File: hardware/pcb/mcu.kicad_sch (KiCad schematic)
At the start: 15 parts, among them J3 FSR pads, U1 ESP32-WROOM-32E-N8R2, U18 W25Q512JVEIQ, U19 TCA6408ARSVR

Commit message: Improve hw_v2 PCB: HV tail chains, decoupling re-park, power islands, U22 escape
Schematic fixes:
- Fix SWEAT_RE silently shorted to GND (D27 pin-endpoint collision)
- Fix L2/TX_5V boost miswire (VBAT_SYS->TX_SW, rail was dead)
- Add J11/J13 HV-boundary chains: R118-R122 2512 cut-points + D26-D30 DNP TPD clamps
- Correct J12 to FH12-14S-0.5SH land; R114 LED_AN fed from TX_5V
- Move U24 VBACKUP to dedicated RTC_VBK net; ADS1292 CLK grounded
- Add CS pull-ups (R115-R117), TP28, C84 (U4 +3V3 input decoupling)
- New hw_v2 parts: U22 MAX86178, U23 SHT45, U24 RTC (DNP), U25 IM69D130 (DNP),
  D12 SFH4735 NIR + Q4 gate, J9-J13 tails

Layout:
- Grow board 32->40 mm east; five 2512 HV parts could not fit at 32 mm
- Re-park ~30 decoupling passives adjacent to their ICs
- Replace phantom moat wall slots with a real >=1.0 mm channel
- Own-layer pour keepouts under HV pads; wider stitch-via HV margin
- U22 WLP: drop 28 NC lands (rows B-E) to open B.Cu escape for F-row
- Retarget dead power islands (TX_5V over its 9 loads, +1V8 under LDO, +3V3 at U7)

BOM/CPL: footprint-aware 0R mapping (0402->C17168, 2512->C2908946),
DNP parts excluded, J11/J13 pads DNP'd, U1 MPN corrected.

Gates: placement zero (291 parts), ERC 0, DRC non-unrouted 0
(9 inherent Q1/Q2/Q4 intra-package clearances waived-by-name).
Board remains unrouted by design - research prototype, not fab-ready.

Generated with [Devin](https://devin.ai)

Co-Authored-By: Devin <158243242+devin-ai-integration[bot]@users.noreply.github.com>
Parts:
- removed U1: ESP32-WROOM-32E-N8R2, RF_Module:ESP32-WROOM-32E, symbol vitalq:ESP32-WROOM-32E-R2
- added C78: 100n, Capacitor_SMD:C_0402_1005Metric, symbol vitalq:C
- added R107, R108: 100k, Resistor_SMD:R_0402_1005Metric, symbol vitalq:R
- added U1: ESP32-S3-MINI-1U-N4R2, vitalq:ESP32_S3_MINI_1U, symbol vitalq:ESP32-S3-MINI-1U-N4R2
- added U25: IM69D130, vitalq:IM69D130, symbol vitalq:IM69D130
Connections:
- net +3V3: now also C78.1, U25.2 (VDD)
- net +3V3_ESP: now also U1.3 (3V3)
- net AD5940_GPIO0: now also U1.18 (IO14)
- net ADS1292_DRDY: now also U1.6 (IO2)
- net AFE4900_ADC_RDY: now also U1.25 (IO21)
- net CHG_PG: now also U1.11 (IO7)
- net CS_AD5940: now also U1.19 (IO15)
- net CS_ADS1292: now also U1.14 (IO10)
- net CS_AFE4900: now also U1.22 (IO18)
- net CS_FLASH: now also U1.20 (IO16)
- net ESP_EN: now also U1.45 (EN)
- net ESP_IO0: now also U1.4 (IO0)
- net ESP_RX: now also U1.40 (RXD0)
- net ESP_TX: now also U1.39 (TXD0)
- net EXP_INT: now also U1.7 (IO3)
- net FSR_ADC: now also U1.5 (IO1)
- net GAUGE_ALRT: now also U1.10 (IO6)
- net GND: now also C78.2, R108.2, U1.1 (GND), U1.2 (GND), U1.42 (GND), U1.43 (GND), U1.46 (GND), U1.47 (GND), U1.48 (GND), U1.49 (GND), U1.50 (GND), U1.51 (GND), U1.52 (GND), U1.53 (GND), U1.54 (GND), U1.55 (GND), U1.56 (GND), U1.57 (GND), U1.58 (GND), U1.59 (GND), U1.60 (GND), U1.61 (GND), U1.62 (GND), U1.63 (GND), U1.64 (GND), U1.65 (GND), U25.4 (SELECT), U25.5 (GND)
- net I2C_SCL: now also U1.13 (IO9)
- net I2C_SDA: now also U1.12 (IO8)
- net LSM6_INT1: now also U1.8 (IO4)
- net SPI_MISO: now also U1.17 (IO13)
- net SPI_MOSI: now also U1.15 (IO11)
- net SPI_SCK: now also U1.16 (IO12)
- net STATUS_LED: now also U1.21 (IO17)
- net TMP117_ALERT: now also U1.9 (IO5)
- new net CS_MAX86178: U1.34 (IO38)
- new net MAX86178_INT: U1.35 (IO39)
- new net MIC_CLK: U1.36 (IO40), U25.3 (CLOCK)
- new net MIC_DAT: U1.37 (IO41), U25.1 (DATA)
- new net SPARE_IN: R107.2, R108.1, U1.38 (IO42)
- new net USB_DM_S3: U1.23 (IO19)
- new net USB_DP_S3: U1.24 (IO20)
- new net VBAT: R107.1
- no-connect marks 3 -> 10
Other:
- note added: "ESP32-S3-MINI-1U-N4R2. U.FL antenna: the x<6.5 mm keep-out is gone. 4 MB flash + 2 MB PSRAM inside."
- note added: "IO0 is the boot strap (SW2, R6). IO3 is JTAG-sel; R53 holds EXP_INT high. IO45/IO46 left unstrapped."
- note added: "IO26 is the in-module PSRAM select on N4R2. IO33-37, IO47, IO48 are spare GPIO, left open."
- note added: "R7 keeps CS_AD5940 high at reset. CS pull-ups R52/R98 unchanged; IO15 is not an S3 strap."
- note added: "SPARE_IN: IO42 digital-only; DNP divider = logic VBAT detect only."
- note added: "U25 IM69D130, DNP. PDM on IO40/IO41. 100 nF on VDD (datasheet)."
- note removed: "ESP32-WROOM-32E-N8R2. GPIO16 is PSRAM and stays inside the module."
- note removed: "GPIO2 and GPIO12 are open so the straps stay low. GPIO15 (CS_AD5940) is pulled up."
- note removed: "GPIO6-11 are the module flash bus and have no symbol pins. ADC1 is GPIO36 and GPIO39."
- note removed: "R7 is the only chip-select pull-up. It is required because GPIO15 must be high at reset."

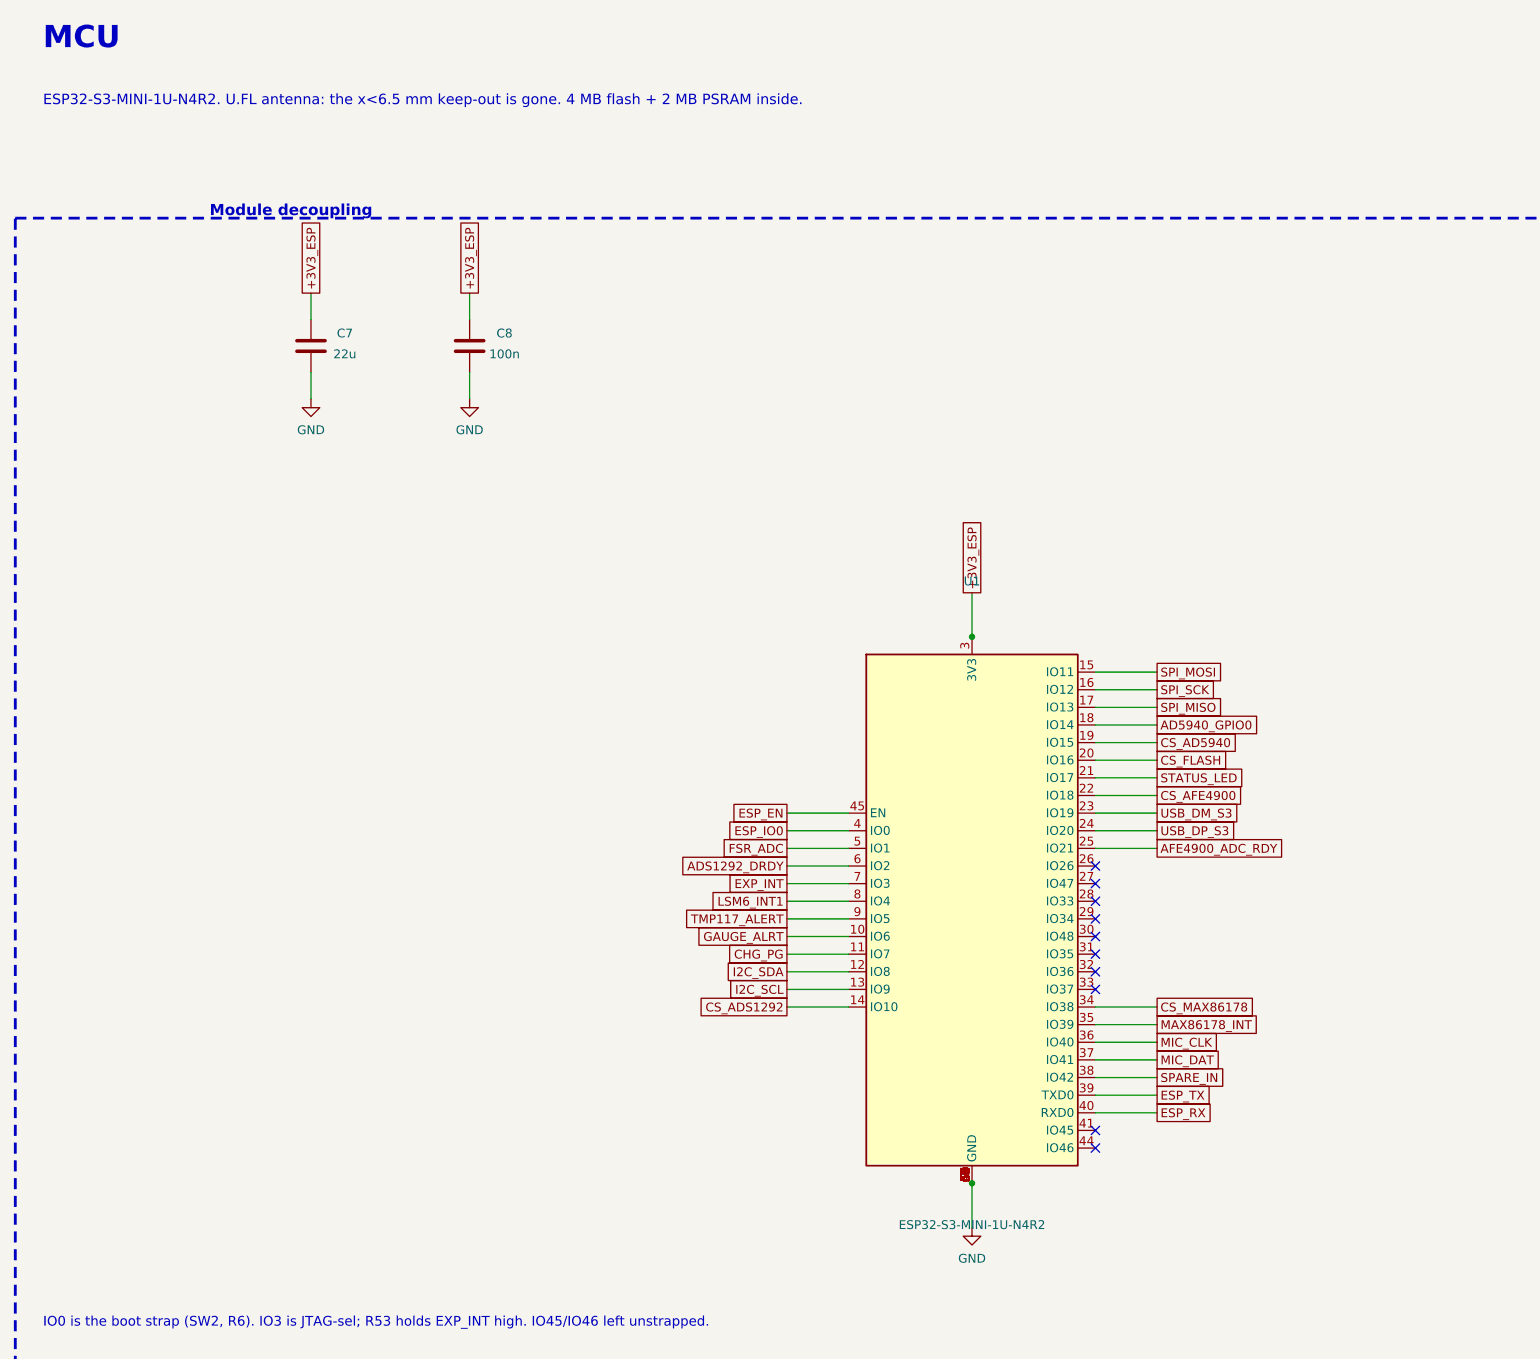
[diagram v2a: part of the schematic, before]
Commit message: Switch U1 to ESP32-S3-MINI-1-N4R2 (integrated PCB antenna)
- design.py: FP_S3 -> vitalq:ESP32_S3_MINI_1; MINI-1 shares the MINI-1U
  65-pad map and N4R2 memory, adds a 5.1 mm pad-free antenna tab
- footprint renamed/extended: outline 15.4x20.5 mm, antenna at local -Y;
  tab overhangs board top edge ~2.8 mm at U1 (12.4, 10.0) rot 0
- build_pcb.py: ufl_dress zone -> antenna_keepout rule area
  (x4.55-20.25, y0-2.45, all copper; no tracks/vias/pads/pours)
- board_finish.py: stitch-via blocklist covers antenna region
- relocations: J9 -> east edge (38.8,15.0,rot90); R7/R70/R71/R72 moved
  out of the keepout band
- BOM/JLC: U1 -> ESP32-S3-MINI-1-N4R2, LCSC C3013941

check.sh: PASS — ERC 0; clashes/edge/pth/pad-miss 0; DRC = 499 unrouted
items only (no keepout violations); 0 vias in antenna zone.

Generated with [Devin](https://devin.ai)

Co-Authored-By: Devin <158243242+devin-ai-integration[bot]@users.noreply.github.com>
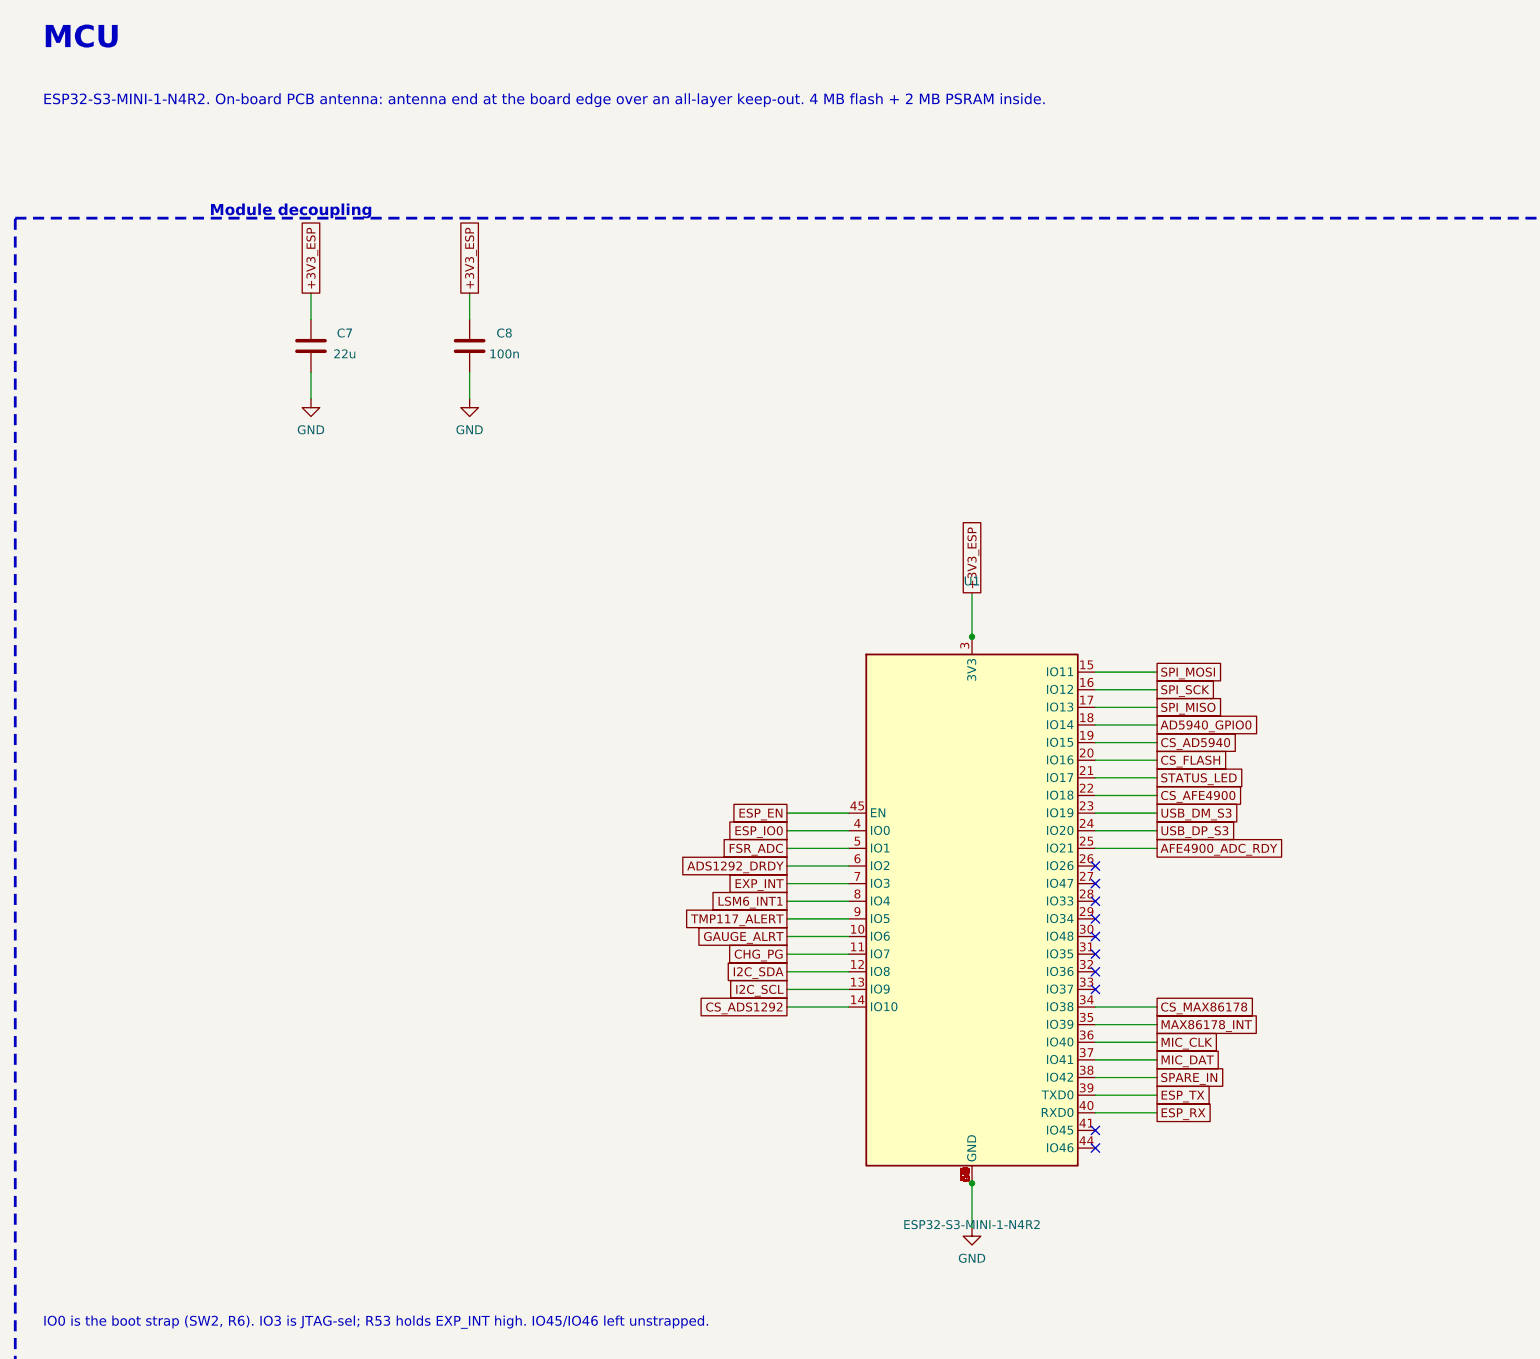
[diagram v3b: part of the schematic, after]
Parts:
- removed U1: ESP32-S3-MINI-1U-N4R2, vitalq:ESP32_S3_MINI_1U, symbol vitalq:ESP32-S3-MINI-1U-N4R2
- added U1: ESP32-S3-MINI-1-N4R2, vitalq:ESP32_S3_MINI_1, symbol vitalq:ESP32-S3-MINI-1-N4R2
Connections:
- net +3V3_ESP: now also U1.3 (3V3)
- net AD5940_GPIO0: now also U1.18 (IO14)
- net ADS1292_DRDY: now also U1.6 (IO2)
- net AFE4900_ADC_RDY: now also U1.25 (IO21)
- net CHG_PG: now also U1.11 (IO7)
- net CS_AD5940: now also U1.19 (IO15)
- net CS_ADS1292: now also U1.14 (IO10)
- net CS_AFE4900: now also U1.22 (IO18)
- net CS_FLASH: now also U1.20 (IO16)
- net CS_MAX86178: now also U1.34 (IO38)
- net ESP_EN: now also U1.45 (EN)
- net ESP_IO0: now also U1.4 (IO0)
- net ESP_RX: now also U1.40 (RXD0)
- net ESP_TX: now also U1.39 (TXD0)
- net EXP_INT: now also U1.7 (IO3)
- net FSR_ADC: now also U1.5 (IO1)
- net GAUGE_ALRT: now also U1.10 (IO6)
- net GND: now also U1.1 (GND), U1.2 (GND), U1.42 (GND), U1.43 (GND), U1.46 (GND), U1.47 (GND), U1.48 (GND), U1.49 (GND), U1.50 (GND), U1.51 (GND), U1.52 (GND), U1.53 (GND), U1.54 (GND), U1.55 (GND), U1.56 (GND), U1.57 (GND), U1.58 (GND), U1.59 (GND), U1.60 (GND), U1.61 (GND), U1.62 (GND), U1.63 (GND), U1.64 (GND), U1.65 (GND)
- net I2C_SCL: now also U1.13 (IO9)
- net I2C_SDA: now also U1.12 (IO8)
- net LSM6_INT1: now also U1.8 (IO4)
- net MAX86178_INT: now also U1.35 (IO39)
- net MIC_CLK: now also U1.36 (IO40)
- net MIC_DAT: now also U1.37 (IO41)
- net SPARE_IN: now also U1.38 (IO42)
- net SPI_MISO: now also U1.17 (IO13)
- net SPI_MOSI: now also U1.15 (IO11)
- net SPI_SCK: now also U1.16 (IO12)
- net STATUS_LED: now also U1.21 (IO17)
- net TMP117_ALERT: now also U1.9 (IO5)
- net USB_DM_S3: now also U1.23 (IO19)
- net USB_DP_S3: now also U1.24 (IO20)
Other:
- note added: "ESP32-S3-MINI-1-N4R2. On-board PCB antenna: antenna end at the board edge over an all-layer keep-out. 4 MB flash + 2 MB PSRAM inside."
- note removed: "ESP32-S3-MINI-1U-N4R2. U.FL antenna: the x<6.5 mm keep-out is gone. 4 MB flash + 2 MB PSRAM inside."
